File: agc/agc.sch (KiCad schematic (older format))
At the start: 113 parts, among them J1 SMA_DAC, J2 SMA_LPTR, J3 SMA_DRIVER, J4 SMA_RX, J5 SIL10, J6 SMA_LPTR, K1 TR, K2 TR, K3 VIN, K4 VOUT_TR, K5 TR, K7 HVMON, P10 CONN_2, P2 FWD_FAULT, P3 REF_FAULT, P4 CONN_8X2, P5 COUPLED_TEST, P6 TP_VCC, P7 COUPLED_TEST, P8 COUPLED_TEST, P9 COUPLED_TEST, U1 BA08CC0WFP, U10 74AHC1G04, U11 74AHC1G04, U12 78SRH-5/2-C, U14 SMP1330-005LF, U15 SMP1330-005LF, U16 SMP1330-005LF, U2 HMC475, U3 HMC595, U4 HMC595, U5 HMC595, U6 74AHC1G04, U7 ISL3281E, U8 MGA-61563, U9 LTC2914-2

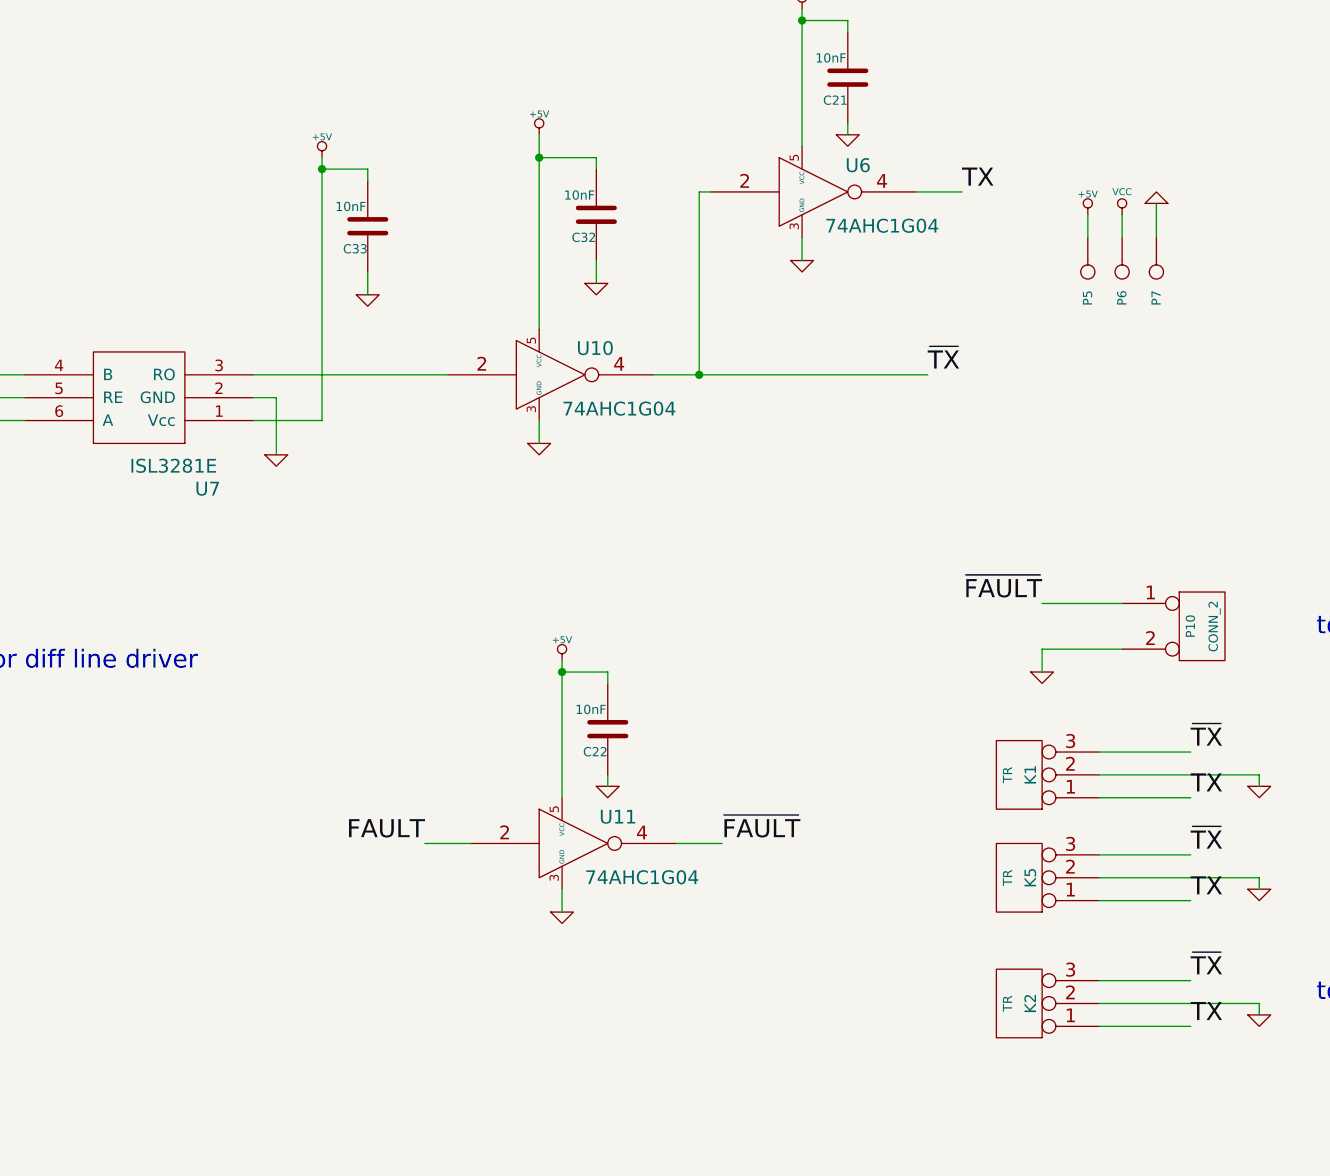
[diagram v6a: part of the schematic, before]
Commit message: added power on reset PMIC to LE on RXFE attenuator
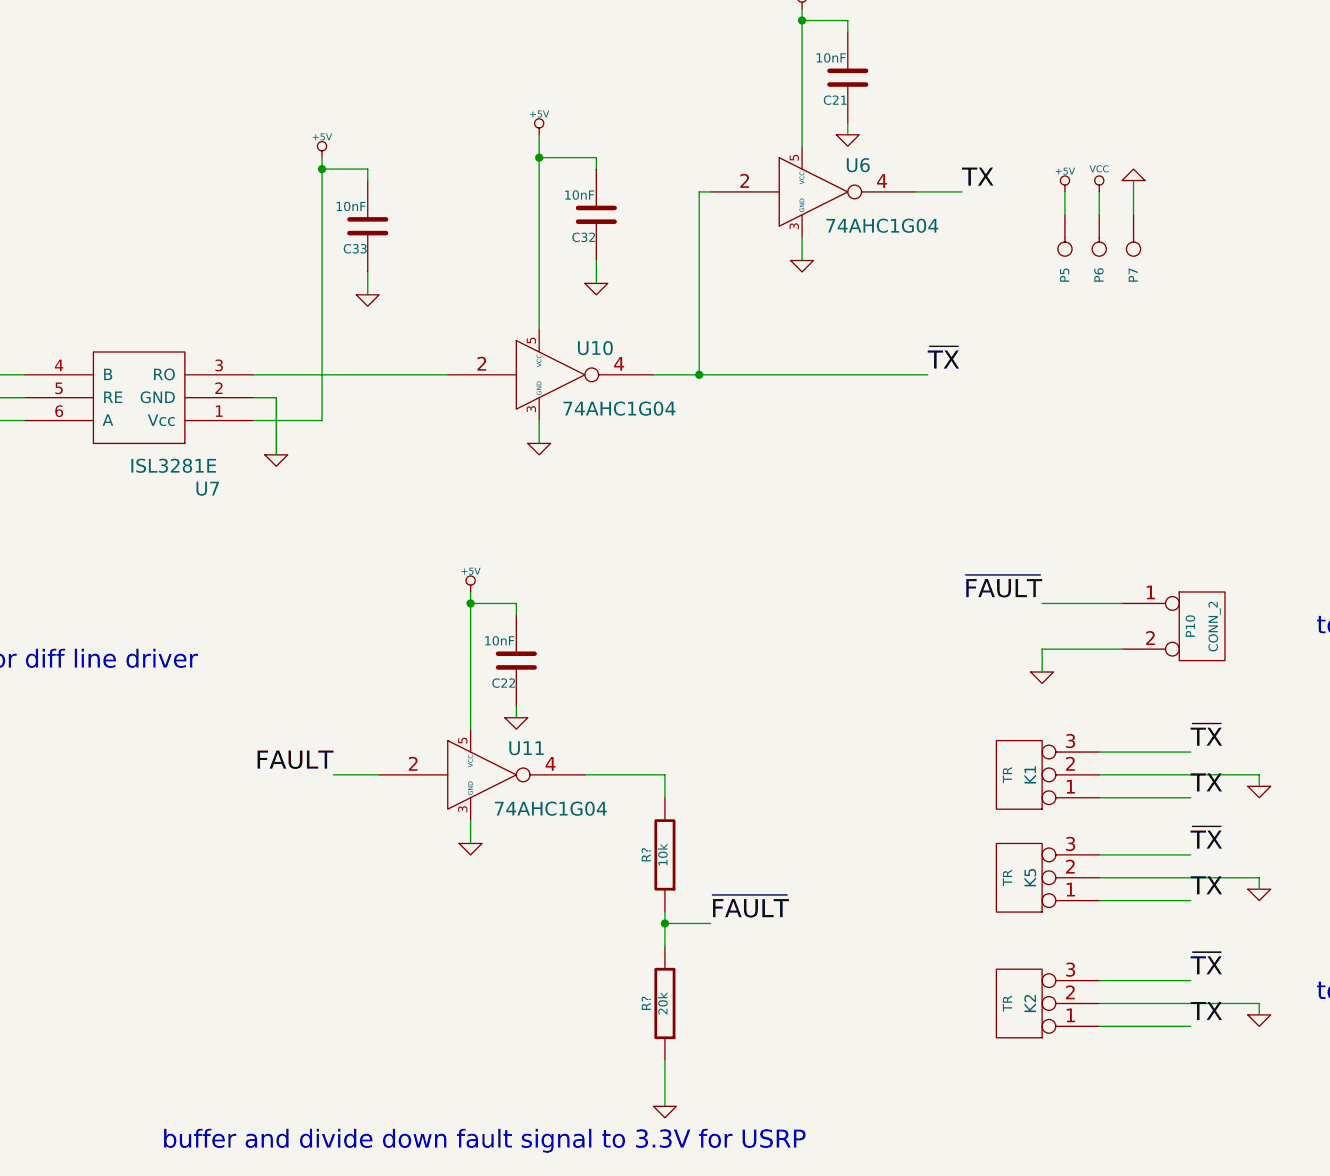
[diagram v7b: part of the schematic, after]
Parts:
- added R?: 10k, SMD_Packages:SM0805, symbol R
- added R?: 20k, SMD_Packages:SM0805, symbol R
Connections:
- net GND: now also R?.1
- net ~FAULT: now also R?.1, R?.2; no longer U11.4
- new net: R?.2, U11.4
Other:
- note added: "buffer and divide down fault signal to 3.3V for USRP"
- moved on the sheet: C22, P5, P6, P7, U11
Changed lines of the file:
@@
 L CONN_1 P5
 U 1 1 53AB611F
-P 14800 12100
-F 0 "P5" H 14880 12100 40  0000 L CNN
-F 1 "COUPLED_TEST" H 14800 12155 30  0001 C CNN
-F 2 "Connect:PINTST" H 14800 12100 60  0001 C CNN
-F 3 "" H 14800 12100 60  0000 C CNN
-	1    14800 12100
+P 14700 12000
+F 0 "P5" H 14780 12000 40  0000 L CNN
+F 1 "COUPLED_TEST" H 14700 12055 30  0001 C CNN
+F 2 "Connect:PINTST" H 14700 12000 60  0001 C CNN
+F 3 "" H 14700 12000 60  0000 C CNN
+	1    14700 12000
 	0    1    1    0
 $EndComp
@@
 L +5V #PWR76
 U 1 1 53AB612A
-P 14800 11850
-F 0 "#PWR76" H 14800 11940 20  0001 C CNN
-F 1 "+5V" H 14800 11940 30  0000 C CNN
-F 2 "" H 14800 11850 60  0000 C CNN
-F 3 "" H 14800 11850 60  0000 C CNN
-	1    14800 11850
+P 14700 11750
+F 0 "#PWR76" H 14700 11840 20  0001 C CNN
+F 1 "+5V" H 14700 11840 30  0000 C CNN
+F 2 "" H 14700 11750 60  0000 C CNN
+F 3 "" H 14700 11750 60  0000 C CNN
+	1    14700 11750
 	1    0    0    -1
 $EndComp
@@
 L CONN_1 P6
 U 1 1 53AB613F
-P 14950 12100
-F 0 "P6" H 15030 12100 40  0000 L CNN
-F 1 "TP_VCC" H 14950 12155 30  0001 C CNN
-F 2 "Connect:PINTST" H 14950 12100 60  0001 C CNN
-F 3 "" H 14950 12100 60  0000 C CNN
-	1    14950 12100
+P 14850 12000
+F 0 "P6" H 14930 12000 40  0000 L CNN
+F 1 "TP_VCC" H 14850 12055 30  0001 C CNN
+F 2 "Connect:PINTST" H 14850 12000 60  0001 C CNN
+F 3 "" H 14850 12000 60  0000 C CNN
+	1    14850 12000
 	0    1    1    0
 $EndComp
@@
 L CONN_1 P7
 U 1 1 53AB614A
-P 15100 12100
-F 0 "P7" H 15180 12100 40  0000 L CNN
-F 1 "COUPLED_TEST" H 15100 12155 30  0001 C CNN
-F 2 "Connect:PINTST" H 15100 12100 60  0001 C CNN
-F 3 "" H 15100 12100 60  0000 C CNN
-	1    15100 12100
+P 15000 12000
+F 0 "P7" H 15080 12000 40  0000 L CNN
+F 1 "COUPLED_TEST" H 15000 12055 30  0001 C CNN
+F 2 "Connect:PINTST" H 15000 12000 60  0001 C CNN
+F 3 "" H 15000 12000 60  0000 C CNN
+	1    15000 12000
 	0    1    1    0
 $EndComp
@@
 L VCC #PWR78
 U 1 1 53AB6155
-P 14950 11850
-F 0 "#PWR78" H 14950 11950 30  0001 C CNN
-F 1 "VCC" H 14950 11950 30  0000 C CNN
-F 2 "" H 14950 11850 60  0000 C CNN
-F 3 "" H 14950 11850 60  0000 C CNN
-	1    14950 11850
+P 14850 11750
+F 0 "#PWR78" H 14850 11850 30  0001 C CNN
+F 1 "VCC" H 14850 11850 30  0000 C CNN
+F 2 "" H 14850 11750 60  0000 C CNN
+F 3 "" H 14850 11750 60  0000 C CNN
+	1    14850 11750
 	1    0    0    -1
 $EndComp
@@
 L GND #PWR80
 U 1 1 53AB65ED
-P 15100 11800
-F 0 "#PWR80" H 15100 11800 30  0001 C CNN
-F 1 "GND" H 15100 11730 30  0001 C CNN
-F 2 "" H 15100 11800 60  0000 C CNN
-F 3 "" H 15100 11800 60  0000 C CNN
-	1    15100 11800
+P 15000 11700
+F 0 "#PWR80" H 15000 11700 30  0001 C CNN
+F 1 "GND" H 15000 11630 30  0001 C CNN
+F 2 "" H 15000 11700 60  0000 C CNN
+F 3 "" H 15000 11700 60  0000 C CNN
+	1    15000 11700
 	-1   0    0    1
 $EndComp
@@
 	16300 10150 18300 10150
 Wire Wire Line
-	14800 11850 14800 11950
-Wire Wire Line
-	14950 11850 14950 11950
-Wire Wire Line
-	15100 11800 15100 11950
+	14700 11750 14700 11850
+Wire Wire Line
+	14850 11750 14850 11850
+Wire Wire Line
+	15000 11700 15000 11850
 Wire Wire Line
 	9100 9550 9100 9650
@@
 L 74AHC1G04 U11
 U 1 1 53BDC592
-P 12550 14600
-F 0 "U11" H 12745 14715 60  0000 C CNN
-F 1 "74AHC1G04" H 12850 14450 60  0000 C CNN
-F 2 "SMD_Packages:SOT23-5" H 12550 14600 60  0001 C CNN
-F 3 "" H 12550 14600 60  0000 C CNN
-	1    12550 14600
+P 12150 14300
+F 0 "U11" H 12345 14415 60  0000 C CNN
+F 1 "74AHC1G04" H 12450 14150 60  0000 C CNN
+F 2 "SMD_Packages:SOT23-5" H 12150 14300 60  0001 C CNN
+F 3 "" H 12150 14300 60  0000 C CNN
+	1    12150 14300
 	1    0    0    -1
 $EndComp
@@
 L GND #PWR63
 U 1 1 53BDC598
-P 12500 14900
-F 0 "#PWR63" H 12500 14900 30  0001 C CNN
-F 1 "GND" H 12500 14830 30  0001 C CNN
-F 2 "" H 12500 14900 60  0000 C CNN
-F 3 "" H 12500 14900 60  0000 C CNN
-	1    12500 14900
+P 12100 14600
+F 0 "#PWR63" H 12100 14600 30  0001 C CNN
+F 1 "GND" H 12100 14530 30  0001 C CNN
+F 2 "" H 12100 14600 60  0000 C CNN
+F 3 "" H 12100 14600 60  0000 C CNN
+	1    12100 14600
 	1    0    0    -1
 $EndComp
@@
 L +5V #PWR62
 U 1 1 53BDC59E
-P 12500 13800
-F 0 "#PWR62" H 12500 13890 20  0001 C CNN
-F 1 "+5V" H 12500 13890 30  0000 C CNN
-F 2 "" H 12500 13800 60  0000 C CNN
-F 3 "" H 12500 13800 60  0000 C CNN
-	1    12500 13800
+P 12100 13500
+F 0 "#PWR62" H 12100 13590 20  0001 C CNN
+F 1 "+5V" H 12100 13590 30  0000 C CNN
+F 2 "" H 12100 13500 60  0000 C CNN
+F 3 "" H 12100 13500 60  0000 C CNN
+	1    12100 13500
 	1    0    0    -1
 $EndComp
@@
 L C C22
 U 1 1 53BDC5A4
-P 12700 14100
-F 0 "C22" H 12700 14200 40  0000 L CNN
-F 1 "10nF" H 12706 14015 40  0000 L CNN
-F 2 "SMD_Packages:SM0805" H 12738 13950 30  0001 C CNN
-F 3 "" H 12700 14100 60  0000 C CNN
-	1    12700 14100
+P 12300 13800
+F 0 "C22" H 12300 13900 40  0000 L CNN
+F 1 "10nF" H 12306 13715 40  0000 L CNN
+F 2 "SMD_Packages:SM0805" H 12338 13650 30  0001 C CNN
+F 3 "" H 12300 13800 60  0000 C CNN
+	1    12300 13800
 	-1   0    0    1
 $EndComp
@@
 L GND #PWR65
 U 1 1 53BDC5AA
-P 12700 14350
-F 0 "#PWR65" H 12700 14350 30  0001 C CNN
-F 1 "GND" H 12700 14280 30  0001 C CNN
-F 2 "" H 12700 14350 60  0000 C CNN
-F 3 "" H 12700 14350 60  0000 C CNN
-	1    12700 14350
-	1    0    0    -1
-$EndComp
-Wire Wire Line
-	12500 14900 12500 14800
-Wire Wire Line
-	13200 14600 13000 14600
-Wire Wire Line
-	12500 13800 12500 14400
-Wire Wire Line
-	12700 14350 12700 14300
-Wire Wire Line
-	12500 13850 12700 13850
-Wire Wire Line
-	12700 13850 12700 13900
-Connection ~ 12500 13850
-Text Label 11900 14600 2    79   ~ 0
+P 12300 14050
+F 0 "#PWR65" H 12300 14050 30  0001 C CNN
+F 1 "GND" H 12300 13980 30  0001 C CNN
+F 2 "" H 12300 14050 60  0000 C CNN
+F 3 "" H 12300 14050 60  0000 C CNN
+	1    12300 14050
+	1    0    0    -1
+$EndComp
+Wire Wire Line
+	12100 14600 12100 14500
+Wire Wire Line
+	12600 14300 12950 14300
+Wire Wire Line
+	12100 13500 12100 14100
+Wire Wire Line
+	12300 14050 12300 14000
+Wire Wire Line
+	12100 13550 12300 13550
+Wire Wire Line
+	12300 13550 12300 13600
+Connection ~ 12100 13550
+Text Label 11500 14300 2    79   ~ 0
 FAULT
 Wire Wire Line
-	11900 14600 12100 14600
-Text Label 13200 14600 0    79   ~ 0
+	11500 14300 11700 14300
+Text Label 13150 14950 0    79   ~ 0
 ~FAULT
 Text Label 14600 13550 2    79   ~ 0
@@
 Text Notes 17250 8250 0    79   ~ 0
 todo: change resistors for 15V
+$Comp
+L R R?
+U 1 1 54247ADB
+P 12950 14650
+F 0 "R?" V 13030 14650 40  0000 C CNN
+F 1 "10k" V 12957 14651 40  0000 C CNN
+F 2 "SMD_Packages:SM0805" V 12880 14650 30  0001 C CNN
+F 3 "" H 12950 14650 30  0000 C CNN
+	1    12950 14650
+	-1   0    0    1
+$EndComp
+$Comp
+L R R?
+U 1 1 54247AED
+P 12950 15300
+F 0 "R?" V 13030 15300 40  0000 C CNN
+F 1 "20k" V 12957 15301 40  0000 C CNN
+F 2 "SMD_Packages:SM0805" V 12880 15300 30  0001 C CNN
+F 3 "" H 12950 15300 30  0000 C CNN
+	1    12950 15300
+	-1   0    0    1
+$EndComp
+Wire Wire Line
+	12950 15550 12950 15750
+$Comp
+L GND #PWR?
+U 1 1 54247CA5
+P 12950 15750
+F 0 "#PWR?" H 12950 15750 30  0001 C CNN
+F 1 "GND" H 12950 15680 30  0001 C CNN
+F 2 "" H 12950 15750 60  0000 C CNN
+F 3 "" H 12950 15750 60  0000 C CNN
+	1    12950 15750
+	1    0    0    -1
+$EndComp
+Wire Wire Line
+	12950 14300 12950 14400
+Wire Wire Line
+	12950 14900 12950 15050
+Wire Wire Line
+	13150 14950 12950 14950
+Connection ~ 12950 14950
+Text Notes 10750 15950 0    79   ~ 0
+buffer and divide down fault signal to 3.3V for USRP
 $EndSCHEMATC

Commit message: moved amp from control board to rxfe
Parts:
- removed C20: DNP, SMD_Packages:SM0805, symbol C
- removed C24, C25, C27: 10nF, SMD_Packages:SM0805, symbol C
- removed C26: 100pF, SMD_Packages:SM0805, symbol C
- removed L4: JMP, SMD_Packages:SM0805, symbol INDUCTOR_SMALL
- removed L5: 10uH, SMD_Packages:SM1210, symbol INDUCTOR_SMALL
- removed R20: 2k2, SMD_Packages:SM0805, symbol R
- removed U8: MGA-61563, Housings_SOT-23_SOT-143_TSOT-6:SC70-6_Handsoldering, symbol MGA-61563
- added H1, H2, H3, H4: MOUNTING_HOLE, Mounting_Holes:MountingHole_3-5mm, symbol MOUNTING_HOLE
- added K6: TR, Connect:PINHEAD1-3, symbol CONN_3
- C1: footprint SMD_Packages:SM0805 -> SMD_Packages:SMD-0805
- J1, J2, J3, J4, J6: footprint sma:sma -> ocal:SMA_5-1814832-1
- P4: footprint Connect:VASCH8x2 -> ocal:conn_8x2
- R4: renamed from R?; value 10k -> JMP; footprint SMD_Packages:SM0805 -> SMD_Packages:SMD-0805
- R5: renamed from R?; footprint SMD_Packages:SM0805 -> SMD_Packages:SMD-0805
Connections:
- net GND: now also K6.2 (PM)
- net TX: now also K6.1 (P1)
- net ~TX: now also K6.3 (P3)
- net at C19.2: now also R22.2, R27.2
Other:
- note removed: "LNA - MGA-61563\n1.5 dB NF at HF\n5V supply\nbias for about 30 mA\n15 dBm P1dB\n"
- note removed: "use rf shield can over rx path?\nsee (952-1475-1-ND) clips\n"
- moved on the sheet: J4, K1, K2, K5, P10, R22, R27, R32, U16
